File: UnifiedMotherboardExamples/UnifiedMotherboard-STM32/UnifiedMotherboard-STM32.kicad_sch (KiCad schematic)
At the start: 1 part, among them U1 Unified Motherboard

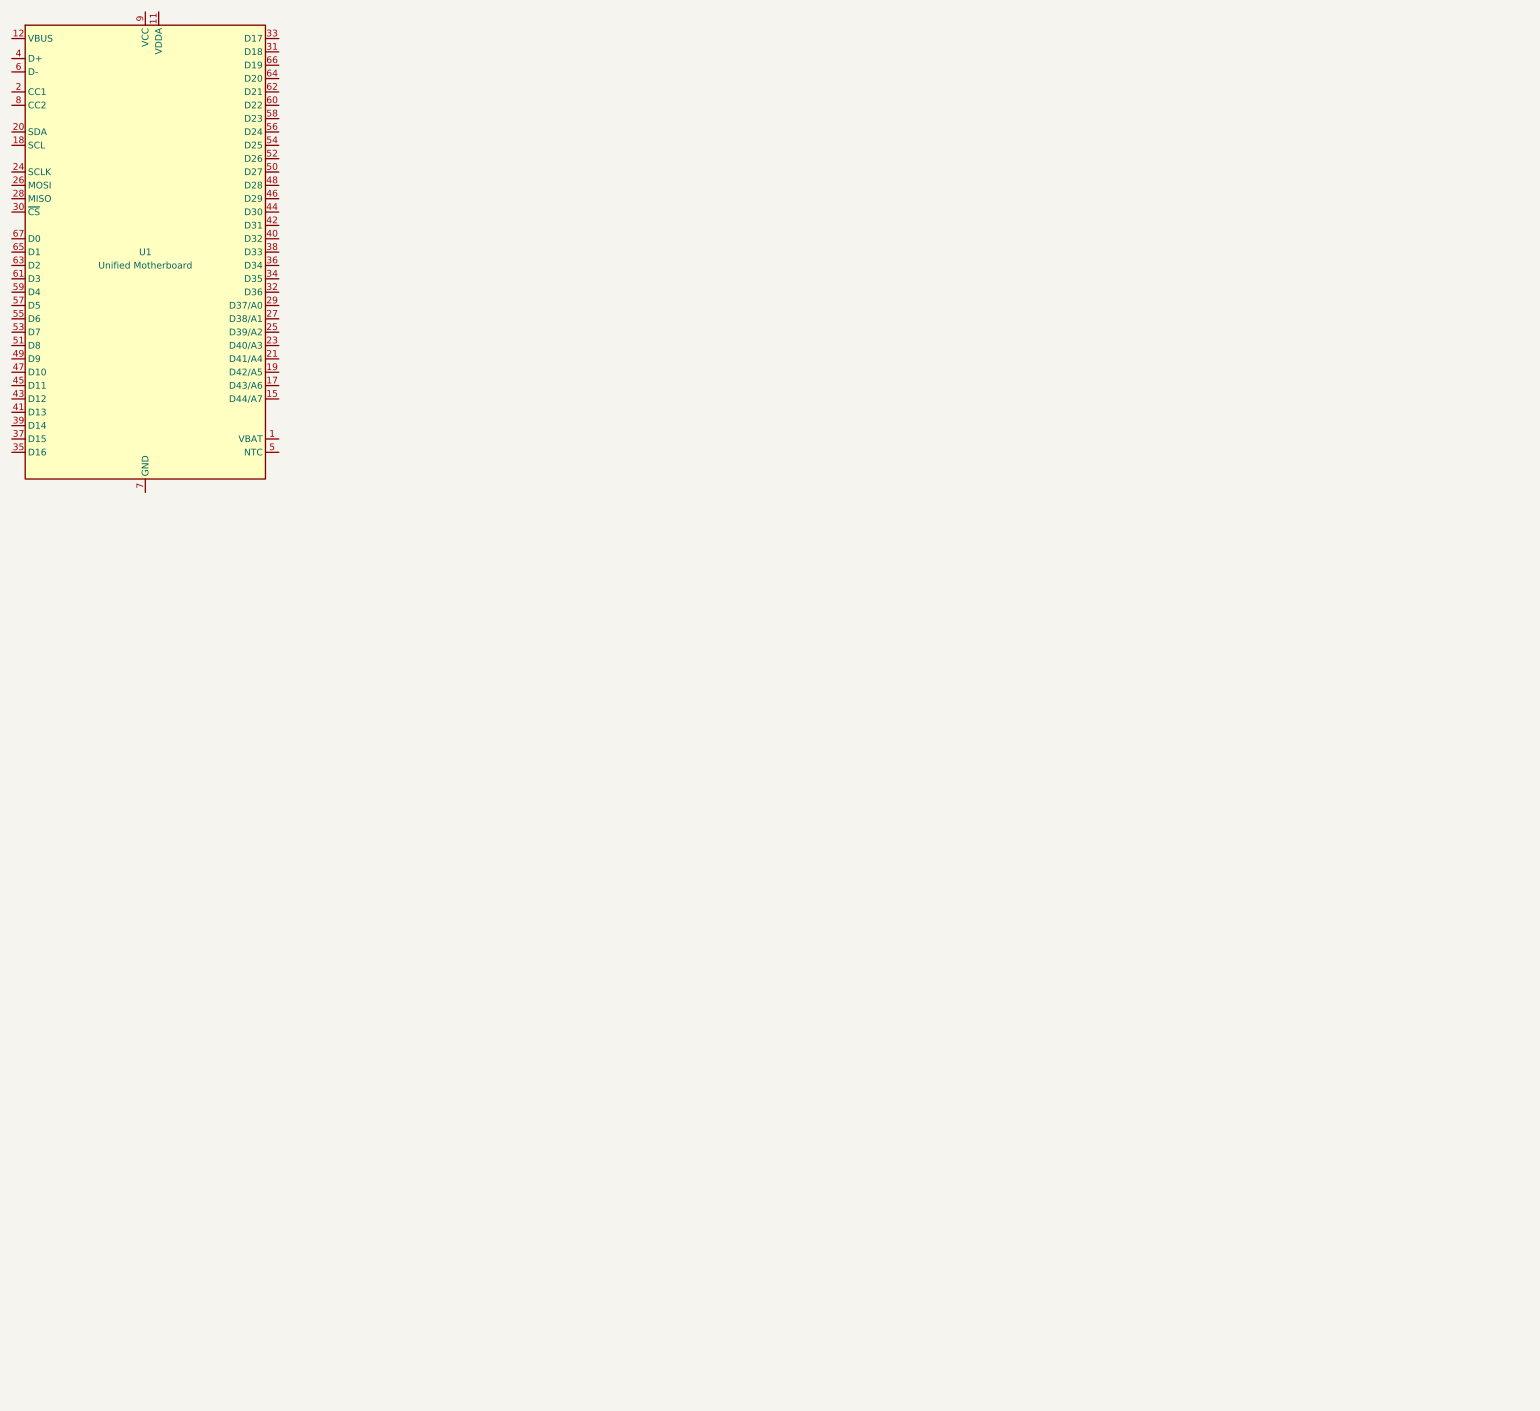
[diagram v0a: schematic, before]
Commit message: Schematic for STM32F072 design
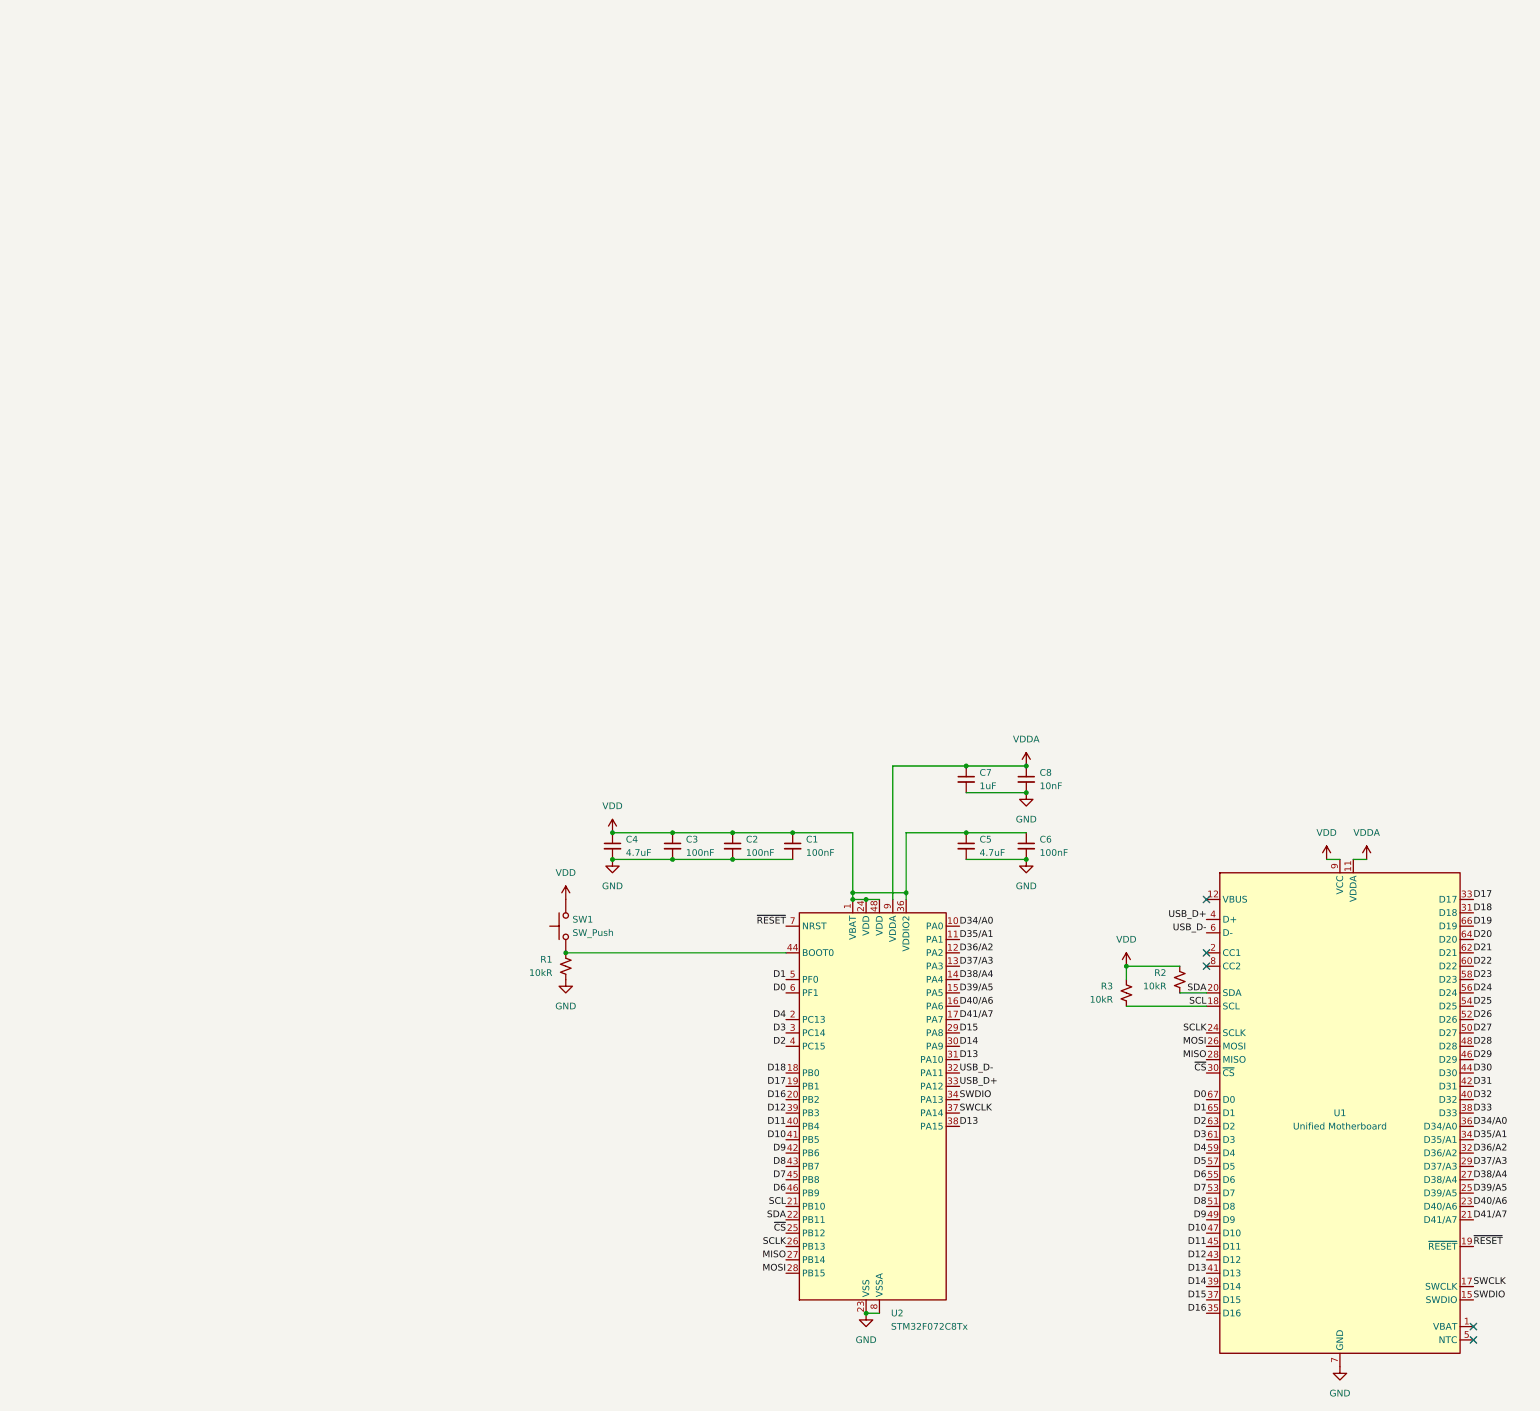
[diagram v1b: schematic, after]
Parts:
- removed U1: Unified Motherboard, UnifiedMotherBoard-Connector_PCBEdge:UnifiedMotherboard, symbol unified_motherboard:UnifiedMotherboard
- added C1, C2, C3, C6: 100nF, Capacitor_SMD:C_0402_1005Metric, symbol Device:C_Small
- added C4, C5: 4.7uF, Capacitor_SMD:C_0805_2012Metric, symbol Device:C_Small
- added C7: 1uF, Capacitor_SMD:C_0402_1005Metric, symbol Device:C_Small
- added C8: 10nF, Capacitor_SMD:C_0402_1005Metric, symbol Device:C_Small
- added R1, R2, R3: 10kR, Resistor_SMD:R_0402_1005Metric, symbol Device:R_Small_US
- added SW1: SW_Push, Button_Switch_SMD:SW_Push_1P1T_NO_Vertical_Wuerth_434133025816, symbol Switch:SW_Push
- added U1: Unified Motherboard, UnifiedMotherBoard-Connector_PCBEdge:UnifiedMotherboard, symbol UnifiedMotherboard:UnifiedMotherboard
- added U2: STM32F072C8Tx, Package_QFP:LQFP-48_7x7mm_P0.5mm, symbol MCU_ST_STM32F0:STM32F072C8Tx
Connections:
- new net: R1.1, SW1.1, U2.44 (BOOT0)
- new net: U1.1 (VBAT), U1.3 (VBAT)
- new net: U1.12 (VBUS), U1.14 (VBUS)
- new net D0: U1.67 (D0), U2.6 (PF1)
- new net D1: U1.65 (D1), U2.5 (PF0)
- new net D10: U1.47 (D10), U2.41 (PB5)
- new net D11: U1.45 (D11), U2.40 (PB4)
- new net D12: U1.43 (D12), U2.39 (PB3)
- new net D13: U1.41 (D13), U2.31 (PA10), U2.38 (PA15)
- new net D14: U1.39 (D14), U2.30 (PA9)
- new net D15: U1.37 (D15), U2.29 (PA8)
- new net D16: U1.35 (D16), U2.20 (PB2)
- new net D17: U1.33 (D17), U2.19 (PB1)
- new net D18: U1.31 (D18), U2.18 (PB0)
- new net D19: U1.66 (D19)
- new net D2: U1.63 (D2), U2.4 (PC15)
- new net D20: U1.64 (D20)
- new net D21: U1.62 (D21)
- new net D22: U1.60 (D22)
- new net D23: U1.58 (D23)
- new net D24: U1.56 (D24)
- new net D25: U1.54 (D25)
- new net D26: U1.52 (D26)
- new net D27: U1.50 (D27)
- new net D28: U1.48 (D28)
- new net D29: U1.46 (D29)
- new net D3: U1.61 (D3), U2.3 (PC14)
- new net D30: U1.44 (D30)
- new net D31: U1.42 (D31)
- new net D32: U1.40 (D32)
- new net D33: U1.38 (D33)
- new net D34/A0: U1.36 (D34/A0), U2.10 (PA0)
- new net D35/A1: U1.34 (D35/A1), U2.11 (PA1)
- new net D36/A2: U1.32 (D36/A2), U2.12 (PA2)
- new net D37/A3: U1.29 (D37/A3), U2.13 (PA3)
- new net D38/A4: U1.27 (D38/A4), U2.14 (PA4)
- new net D39/A5: U1.25 (D39/A5), U2.15 (PA5)
- new net D4: U1.59 (D4), U2.2 (PC13)
- new net D40/A6: U1.23 (D40/A6), U2.16 (PA6)
- new net D41/A7: U1.21 (D41/A7), U2.17 (PA7)
- new net D5: U1.57 (D5)
- new net D6: U1.55 (D6), U2.46 (PB9)
- new net D7: U1.53 (D7), U2.45 (PB8)
- new net D8: U1.51 (D8), U2.43 (PB7)
- new net D9: U1.49 (D9), U2.42 (PB6)
- new net GND: C1.2, C2.2, C3.2, C4.2, C5.2, C6.2, C7.2, C8.2, R1.2, U1.10 (GND), U1.13 (GND), U1.16 (GND), U1.22 (GND), U1.7 (GND), U1.MP, U2.23 (VSS), U2.35 (VSS), U2.47 (VSS), U2.8 (VSSA)
- new net MISO: U1.28 (MISO), U2.27 (PB14)
- new net MOSI: U1.26 (MOSI), U2.28 (PB15)
- new net SCL: R3.2, U1.18 (SCL), U2.21 (PB10)
- new net SCLK: U1.24 (SCLK), U2.26 (PB13)
- new net SDA: R2.2, U1.20 (SDA), U2.22 (PB11)
- new net SWCLK: U1.17 (SWCLK), U2.37 (PA14)
- new net SWDIO: U1.15 (SWDIO), U2.34 (PA13)
- new net USB_D+: U1.4 (D+), U2.33 (PA12)
- new net USB_D-: U1.6 (D-), U2.32 (PA11)
- new net VDD: C1.1, C2.1, C3.1, C4.1, C5.1, C6.1, R2.1, R3.1, SW1.2, U1.9 (VCC), U2.1 (VBAT), U2.24 (VDD), U2.36 (VDDIO2), U2.48 (VDD)
- new net VDDA: C7.1, C8.1, U1.11 (VDDA), U2.9 (VDDA)
- new net ~{CS}: U1.30 (~{CS}), U2.25 (PB12)
- new net ~{RESET}: U1.19 (~{RESET}), U2.7 (NRST)
- no-connect marks 0 -> 5
